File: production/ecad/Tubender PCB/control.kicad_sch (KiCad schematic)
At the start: 42 parts, among them J1 USB4110GFA, Q1 AO3400A, Q2 AO3400A, U10 MCP23017-E_SO, U2 ESP32-WROOM-32UE_M113EH6400UH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, U3 MCP23017-E_SO, U4 FT232RL-REEL

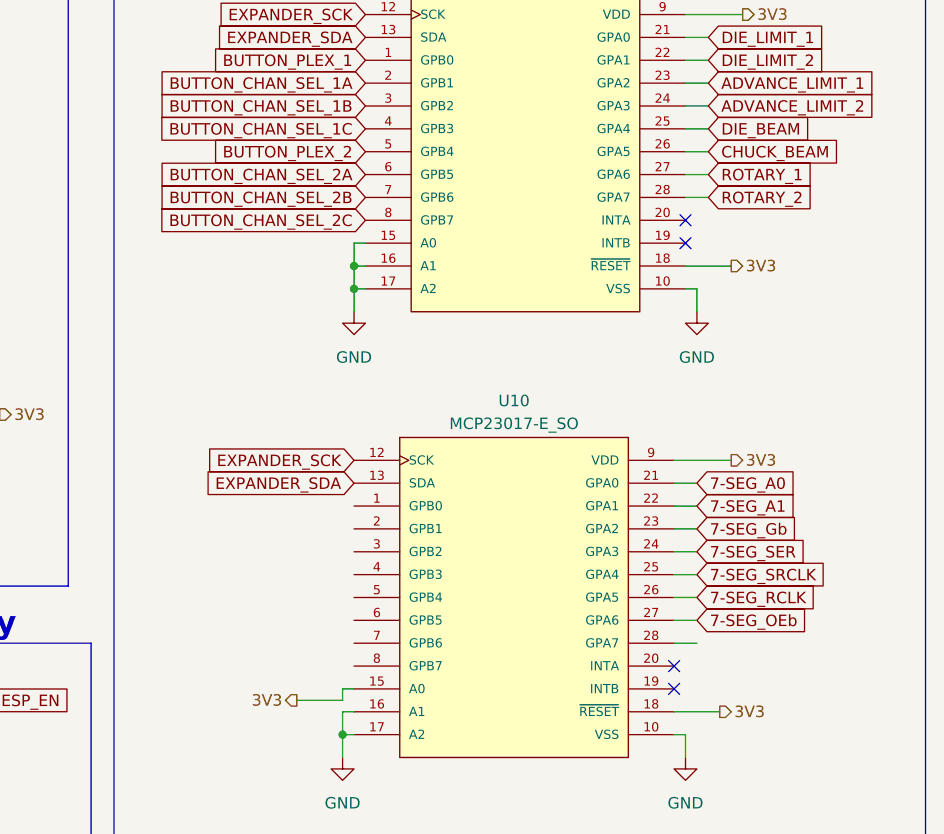
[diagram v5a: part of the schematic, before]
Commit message: Display to MCU
Forgot to add global nets for display to the control page, my b
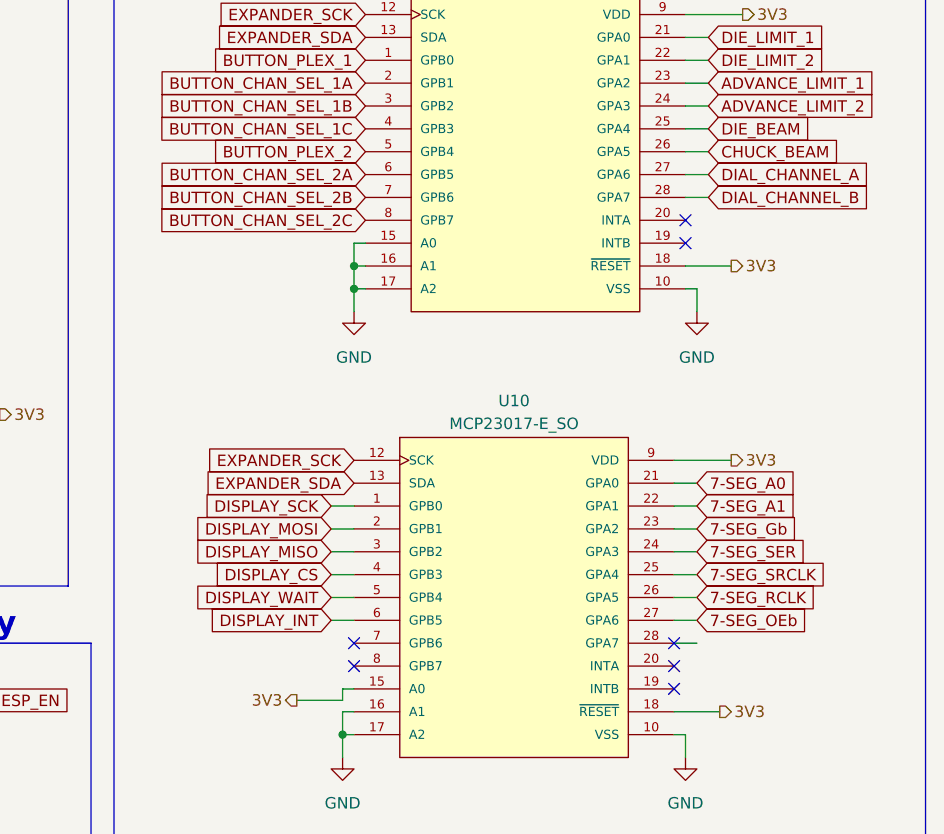
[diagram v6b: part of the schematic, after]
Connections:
- net DISPLAY_SCK: now reaches U10.1 (GPB0)
- net DISPLAY_MOSI: now reaches U10.2 (GPB1)
- net DISPLAY_MISO: now reaches U10.3 (GPB2)
- net DISPLAY_CS: now reaches U10.4 (GPB3)
- net DISPLAY_WAIT: now reaches U10.5 (GPB4)
- net DISPLAY_INT: now reaches U10.6 (GPB5)
- net ROTARY_1 renamed DIAL_CHANNEL_A
- net ROTARY_2 renamed DIAL_CHANNEL_B
- no-connect marks 14 -> 17
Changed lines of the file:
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@@
 	)
 	(no_connect
+		(at 218.44 101.6)
+	)
+	(no_connect
 		(at 152.4 57.15)
 	)
@@
 	)
 	(no_connect
+		(at 218.44 99.06)
+	)
+	(no_connect
 		(at 152.4 59.69)
 	)
@@
 	)
 	(no_connect
+		(at 254 99.06)
+	)
+	(no_connect
 		(at 121.92 44.45)
 	)
@@
 	(wire
 		(pts
+			(xy 215.9 93.98) (xy 218.44 93.98)
+		)
+		(stroke
+			(width 0)
+			(type default)
+		)
+	)
+	(wire
+		(pts
 			(xy 256.54 59.69) (xy 255.27 59.69)
 		)
@@
 	(wire
 		(pts
+			(xy 215.9 83.82) (xy 218.44 83.82)
+		)
+		(stroke
+			(width 0)
+			(type default)
+		)
+	)
+	(wire
+		(pts
 			(xy 157.48 64.77) (xy 152.4 64.77)
 		)
@@
 	(wire
 		(pts
+			(xy 215.9 96.52) (xy 218.44 96.52)
+		)
+		(stroke
+			(width 0)
+			(type default)
+		)
+	)
+	(wire
+		(pts
 			(xy 260.35 78.74) (xy 254 78.74)
 		)
@@
 	(wire
 		(pts
+			(xy 215.9 86.36) (xy 218.44 86.36)
+		)
+		(stroke
+			(width 0)
+			(type default)
+		)
+	)
+	(wire
+		(pts
 			(xy 78.74 125.73) (xy 85.09 125.73)
 		)
@@
 	(wire
 		(pts
+			(xy 215.9 88.9) (xy 218.44 88.9)
+		)
+		(stroke
+			(width 0)
+			(type default)
+		)
+	)
+	(wire
+		(pts
 			(xy 120.65 85.09) (xy 121.92 85.09)
 		)
@@
 	(wire
 		(pts
+			(xy 215.9 91.44) (xy 218.44 91.44)
+		)
+		(stroke
+			(width 0)
+			(type default)
+		)
+	)
+	(wire
+		(pts
 			(xy 119.38 34.29) (xy 121.92 34.29)
 		)
@@
 		)
 	)
+	(global_label "DISPLAY_MISO"
+		(shape input)
+		(at 215.9 88.9 180)
+		(fields_autoplaced yes)
+		(effects
+			(font
+				(size 1.27 1.27)
+			)
+			(justify right)
+		)
+		(property "Intersheetrefs" "${INTERSHEET_REFS}"
+			(at 199.7914 88.9 0)
+			(effects
+				(font
+					(size 1.27 1.27)
+				)
+				(justify right)
+				(hide yes)
+			)
+		)
+	)
 	(global_label "GPIO_0"
 		(shape input)
@@
 		)
 	)
-	(global_label "ROTARY_1"
+	(global_label "DIAL_CHANNEL_A"
 		(shape input)
 		(at 257.81 46.99 0)
@@
 		)
 		(property "Intersheetrefs" "${INTERSHEET_REFS}"
-			(at 269.9876 46.99 0)
+			(at 276.3377 46.99 0)
 			(effects
 				(font
@@
 		)
 	)
+	(global_label "DISPLAY_SCK"
+		(shape input)
+		(at 215.9 83.82 180)
+		(fields_autoplaced yes)
+		(effects
+			(font
+				(size 1.27 1.27)
+			)
+			(justify right)
+		)
+		(property "Intersheetrefs" "${INTERSHEET_REFS}"
+			(at 200.6381 83.82 0)
+			(effects
+				(font
+					(size 1.27 1.27)
+				)
+				(justify right)
+				(hide yes)
+			)
+		)
+	)
+	(global_label "DISPLAY_MOSI"
+		(shape input)
+		(at 215.9 86.36 180)
+		(fields_autoplaced yes)
+		(effects
+			(font
+				(size 1.27 1.27)
+			)
+			(justify right)
+		)
+		(property "Intersheetrefs" "${INTERSHEET_REFS}"
+			(at 199.7914 86.36 0)
+			(effects
+				(font
+					(size 1.27 1.27)
+				)
+				(justify right)
+				(hide yes)
+			)
+		)
+	)
 	(global_label "ADVANCING_ENA+"
 		(shape input)
@@
 		)
 	)
+	(global_label "DISPLAY_INT"
+		(shape input)
+		(at 215.9 96.52 180)
+		(fields_autoplaced yes)
+		(effects
+			(font
+				(size 1.27 1.27)
+			)
+			(justify right)
+		)
+		(property "Intersheetrefs" "${INTERSHEET_REFS}"
+			(at 201.4847 96.52 0)
+			(effects
+				(font
+					(size 1.27 1.27)
+				)
+				(justify right)
+				(hide yes)
+			)
+		)
+	)
 	(global_label "EXPANDER_SCK"
 		(shape input)
@@
 		)
 	)
-	(global_label "ROTARY_2"
+	(global_label "DIAL_CHANNEL_B"
 		(shape input)
 		(at 257.81 49.53 0)
@@
 		)
 		(property "Intersheetrefs" "${INTERSHEET_REFS}"
-			(at 269.9876 49.53 0)
+			(at 276.5191 49.53 0)
 			(effects
 				(font
@@
 		)
 	)
+	(global_label "DISPLAY_CS"
+		(shape input)
+		(at 215.9 91.44 180)
+		(fields_autoplaced yes)
+		(effects
+			(font
+				(size 1.27 1.27)
+			)
+			(justify right)
+		)
+		(property "Intersheetrefs" "${INTERSHEET_REFS}"
+			(at 201.9081 91.44 0)
+			(effects
+				(font
+					(size 1.27 1.27)
+				)
+				(justify right)
+				(hide yes)
+			)
+		)
+	)
 	(global_label "ESP_SCK"
 		(shape input)
@@
 				(hide yes)
 			)
+		)
+	)
+	(global_label "DISPLAY_WAIT"
+		(shape input)
+		(at 215.9 93.98 180)
+		(fields_autoplaced yes)
+		(effects
+			(font
+				(size 1.27 1.27)
+			)
+			(justify right)
+		)
+		(property "Intersheetrefs" "${INTERSHEET_REFS}"
+			(at 200.2752 93.98 0)
+			(effects
+				(font
+					(size 1.27 1.27)
+				)
+				(justify right)
+				(hide yes)
+			)

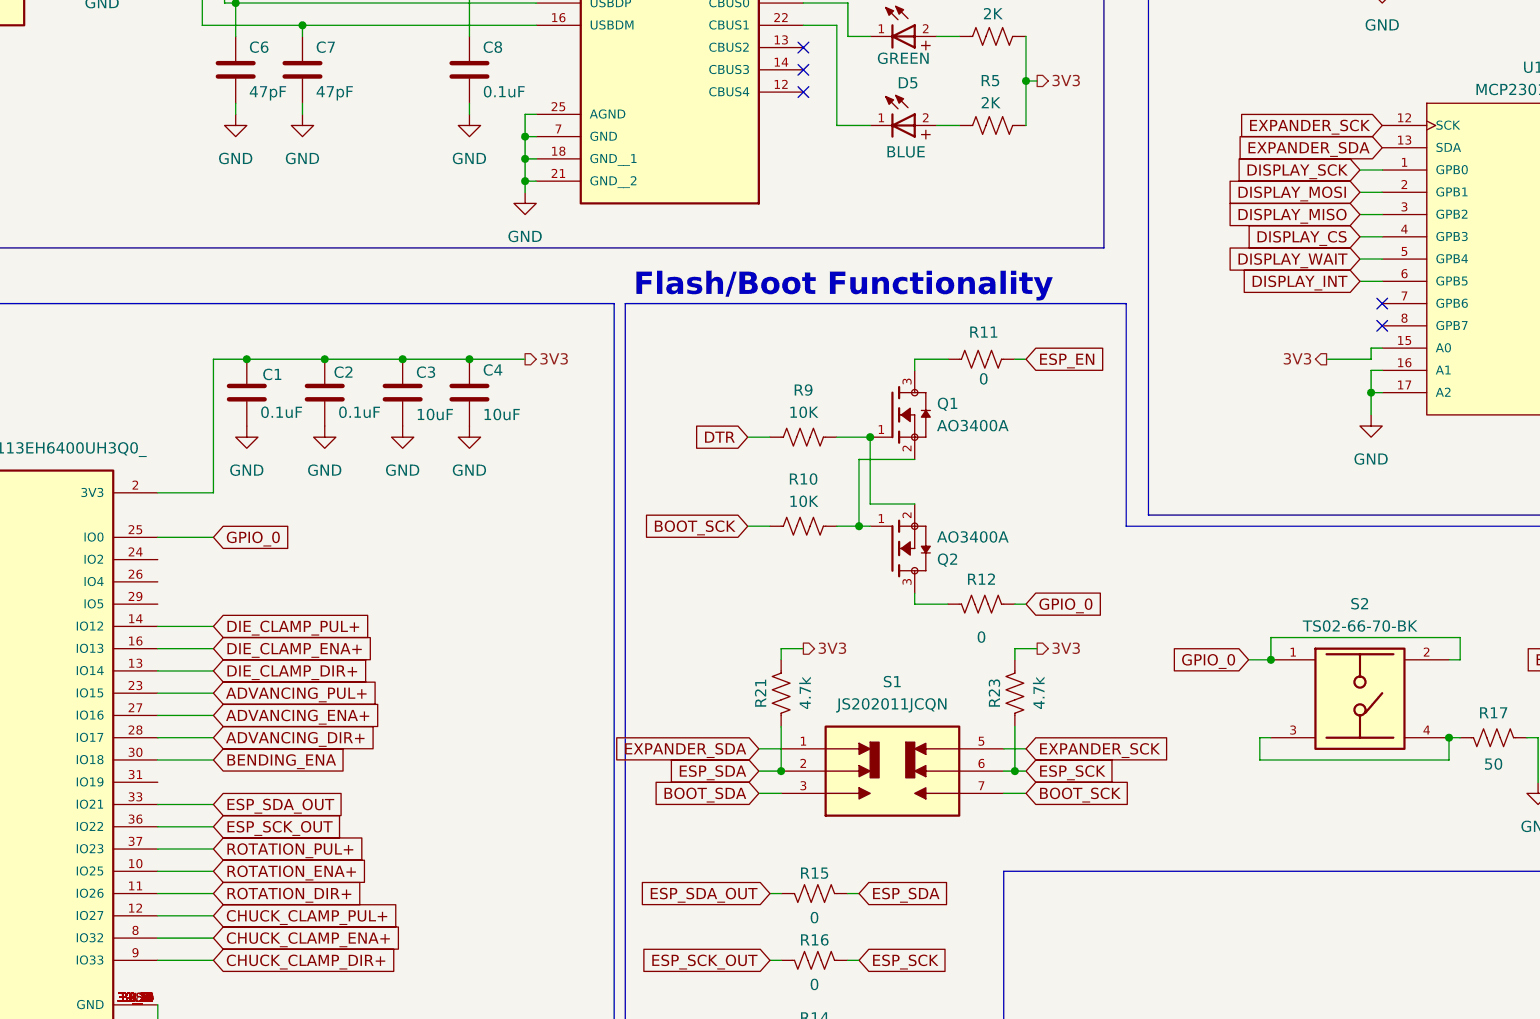
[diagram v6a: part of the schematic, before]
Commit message: Moved Display SPI to MCU VSPI and Organized UI Sheet
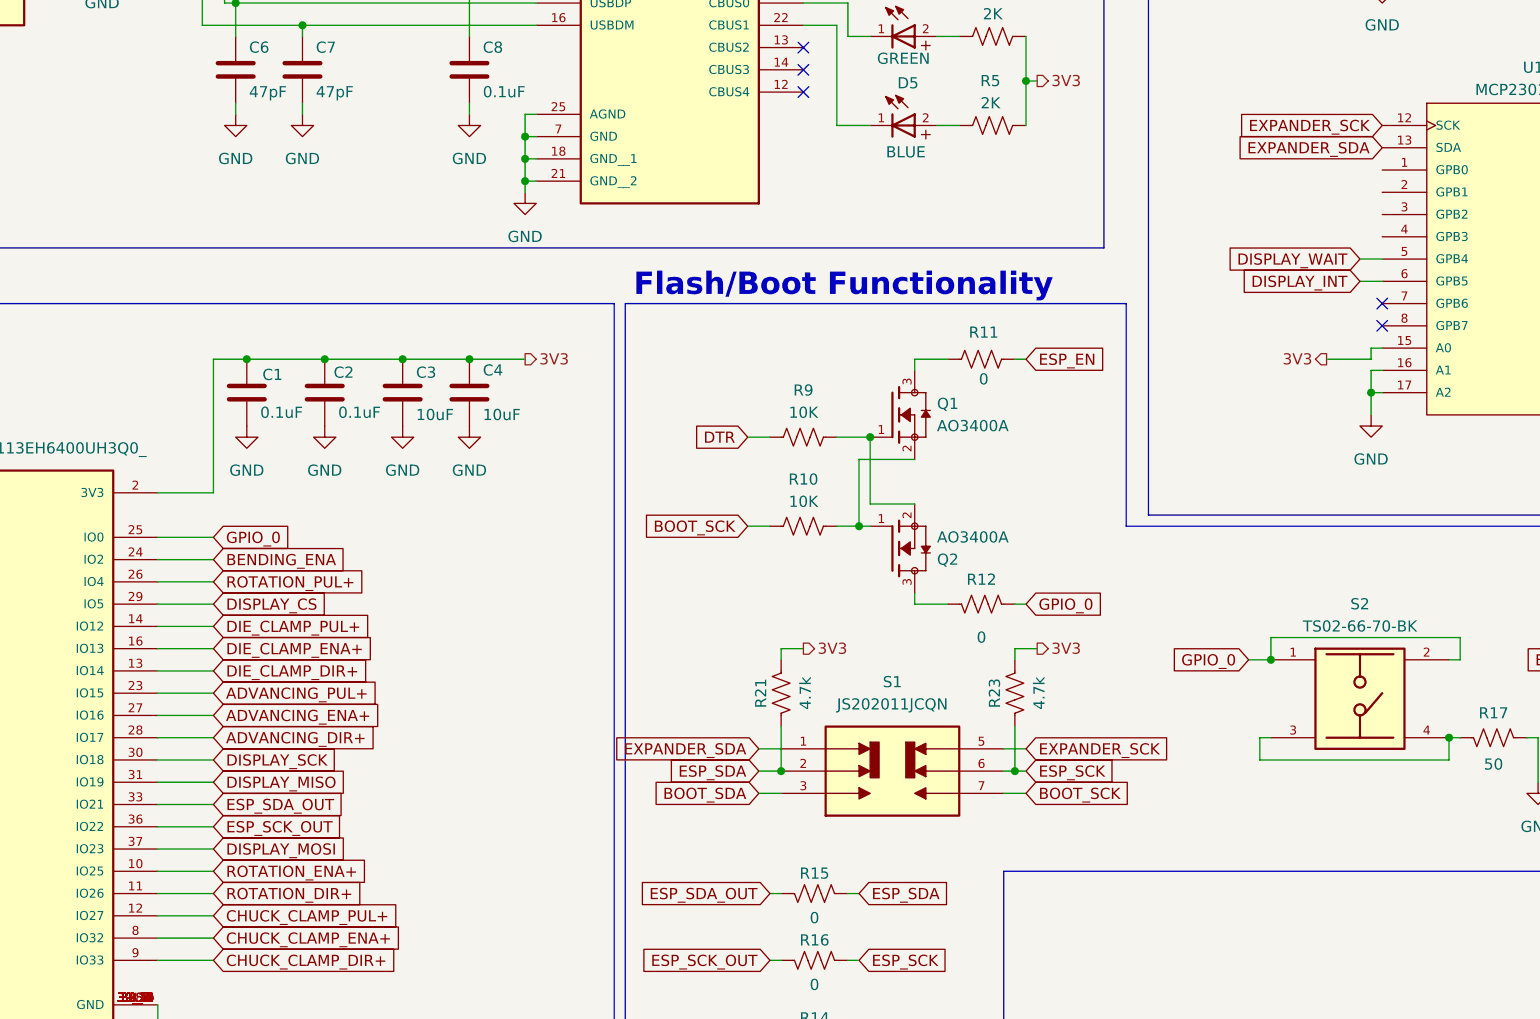
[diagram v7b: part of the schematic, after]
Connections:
- net BENDING_ENA: now also U2.24 (IO2); no longer U2.30 (IO18)
- net DISPLAY_CS: now also U2.29 (IO5); no longer U10.4 (GPB3)
- net DISPLAY_MISO: now also U2.31 (IO19); no longer U10.3 (GPB2)
- net DISPLAY_MOSI: now also U2.37 (IO23); no longer U10.2 (GPB1)
- net DISPLAY_SCK: now also U2.30 (IO18); no longer U10.1 (GPB0)
- net ROTATION_PUL+: now also U2.26 (IO4); no longer U2.37 (IO23)
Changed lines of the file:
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@@
 	(wire
 		(pts
+			(xy 78.74 153.67) (xy 85.09 153.67)
+		)
+		(stroke
+			(width 0)
+			(type default)
+		)
+	)
+	(wire
+		(pts
 			(xy 149.86 138.43) (xy 149.86 139.7)
 		)
@@
 	(wire
 		(pts
-			(xy 85.09 151.13) (xy 78.74 151.13)
+			(xy 255.27 111.76) (xy 255.27 109.22)
 		)
 		(stroke
@@
 	(wire
 		(pts
-			(xy 255.27 111.76) (xy 255.27 109.22)
+			(xy 71.12 31.75) (xy 87.63 31.75)
 		)
 		(stroke
@@
 	(wire
 		(pts
-			(xy 71.12 31.75) (xy 87.63 31.75)
+			(xy 152.4 67.31) (xy 156.21 67.31)
 		)
 		(stroke
@@
 	(wire
 		(pts
-			(xy 152.4 67.31) (xy 156.21 67.31)
+			(xy 218.44 57.15) (xy 219.71 57.15)
 		)
 		(stroke
@@
 	(wire
 		(pts
-			(xy 218.44 57.15) (xy 219.71 57.15)
+			(xy 31.75 125.73) (xy 38.1 125.73)
 		)
 		(stroke
@@
 	(wire
 		(pts
-			(xy 31.75 125.73) (xy 38.1 125.73)
+			(xy 78.74 161.29) (xy 85.09 161.29)
 		)
 		(stroke
@@
 	(wire
 		(pts
-			(xy 215.9 83.82) (xy 218.44 83.82)
-		)
-		(stroke
-			(width 0)
-			(type default)
-		)
-	)
-	(wire
-		(pts
 			(xy 157.48 64.77) (xy 152.4 64.77)
 		)
@@
 	(wire
 		(pts
-			(xy 215.9 86.36) (xy 218.44 86.36)
-		)
-		(stroke
-			(width 0)
-			(type default)
-		)
-	)
-	(wire
-		(pts
 			(xy 78.74 125.73) (xy 85.09 125.73)
 		)
@@
 	(wire
 		(pts
+			(xy 78.74 130.81) (xy 85.09 130.81)
+		)
+		(stroke
+			(width 0)
+			(type default)
+		)
+	)
+	(wire
+		(pts
 			(xy 149.86 147.32) (xy 149.86 152.4)
 		)
@@
 	(wire
 		(pts
-			(xy 85.09 161.29) (xy 78.74 161.29)
-		)
-		(stroke
-			(width 0)
-			(type default)
-		)
-	)
-	(wire
-		(pts
 			(xy 257.81 36.83) (xy 255.27 36.83)
 		)
@@
 	(wire
 		(pts
+			(xy 78.74 128.27) (xy 85.09 128.27)
+		)
+		(stroke
+			(width 0)
+			(type default)
+		)
+	)
+	(wire
+		(pts
 			(xy 85.09 140.97) (xy 78.74 140.97)
 		)
@@
 	(wire
 		(pts
-			(xy 215.9 88.9) (xy 218.44 88.9)
-		)
-		(stroke
-			(width 0)
-			(type default)
-		)
-	)
-	(wire
-		(pts
 			(xy 120.65 85.09) (xy 121.92 85.09)
 		)
@@
 	(wire
 		(pts
+			(xy 78.74 151.13) (xy 85.09 151.13)
+		)
+		(stroke
+			(width 0)
+			(type default)
+		)
+	)
+	(wire
+		(pts
 			(xy 246.38 139.7) (xy 248.92 139.7)
 		)
@@
 	(wire
 		(pts
-			(xy 177.8 149.86) (xy 175.26 149.86)
+			(xy 78.74 133.35) (xy 85.09 133.35)
 		)
 		(stroke
@@
 		)
 	)
-	(polyline
+	(wire
 		(pts
-			(xy 175.26 163.83) (xy 281.94 163.83)
+			(xy 177.8 149.86) (xy 175.26 149.86)
 		)
 		(stroke
@@
 		)
 	)
-	(wire
+	(polyline
 		(pts
-			(xy 215.9 91.44) (xy 218.44 91.44)
+			(xy 175.26 163.83) (xy 281.94 163.83)
 		)
 		(stroke
@@
 	(global_label "DISPLAY_MISO"
 		(shape input)
-		(at 215.9 88.9 180)
+		(at 85.09 153.67 0)
 		(fields_autoplaced yes)
 		(effects
@@
 				(size 1.27 1.27)
 			)
-			(justify right)
+			(justify left)
 		)
 		(property "Intersheetrefs" "${INTERSHEET_REFS}"
-			(at 199.7914 88.9 0)
+			(at 101.1986 153.67 0)
 			(effects
 				(font
 					(size 1.27 1.27)
 				)
-				(justify right)
+				(justify left)
 				(hide yes)
 			)
@@
 	(global_label "DISPLAY_SCK"
 		(shape input)
-		(at 215.9 83.82 180)
+		(at 85.09 151.13 0)
 		(fields_autoplaced yes)
 		(effects
@@
 				(size 1.27 1.27)
 			)
-			(justify right)
+			(justify left)
 		)
 		(property "Intersheetrefs" "${INTERSHEET_REFS}"
-			(at 200.6381 83.82 0)
+			(at 100.3519 151.13 0)
 			(effects
 				(font
 					(size 1.27 1.27)
 				)
-				(justify right)
+				(justify left)
 				(hide yes)
 			)
@@
 	(global_label "DISPLAY_MOSI"
 		(shape input)
-		(at 215.9 86.36 180)
+		(at 85.09 161.29 0)
 		(fields_autoplaced yes)
 		(effects
@@
 				(size 1.27 1.27)
 			)
-			(justify right)
+			(justify left)
 		)
 		(property "Intersheetrefs" "${INTERSHEET_REFS}"
-			(at 199.7914 86.36 0)
+			(at 101.1986 161.29 0)
 			(effects
 				(font
 					(size 1.27 1.27)
 				)
-				(justify right)
+				(justify left)
 				(hide yes)
 			)
@@
 	(global_label "BENDING_ENA"
 		(shape input)
-		(at 85.09 151.13 0)
+		(at 85.09 128.27 0)
 		(fields_autoplaced yes)
 		(effects
@@
 		)
 		(property "Intersheetrefs" "${INTERSHEET_REFS}"
-			(at 100.8357 151.13 0)
+			(at 100.8357 128.27 0)
 			(effects
 				(font
@@
 	(global_label "DISPLAY_CS"
 		(shape input)
-		(at 215.9 91.44 180)
+		(at 85.09 133.35 0)
 		(fields_autoplaced yes)
 		(effects
@@
 				(size 1.27 1.27)
 			)
-			(justify right)
+			(justify left)
 		)
 		(property "Intersheetrefs" "${INTERSHEET_REFS}"
-			(at 201.9081 91.44 0)
+			(at 99.0819 133.35 0)
 			(effects
 				(font
 					(size 1.27 1.27)
 				)
-				(justify right)
+				(justify left)
 				(hide yes)
 			)
@@
 	(global_label "ROTATION_PUL+"
 		(shape input)
-		(at 85.09 161.29 0)
+		(at 85.09 130.81 0)
 		(fields_autoplaced yes)
 		(effects
@@
 		)
 		(property "Intersheetrefs" "${INTERSHEET_REFS}"
-			(at 103.1339 161.29 0)
+			(at 103.1339 130.81 0)
 			(effects
 				(font
